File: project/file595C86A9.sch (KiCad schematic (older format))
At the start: 12 parts

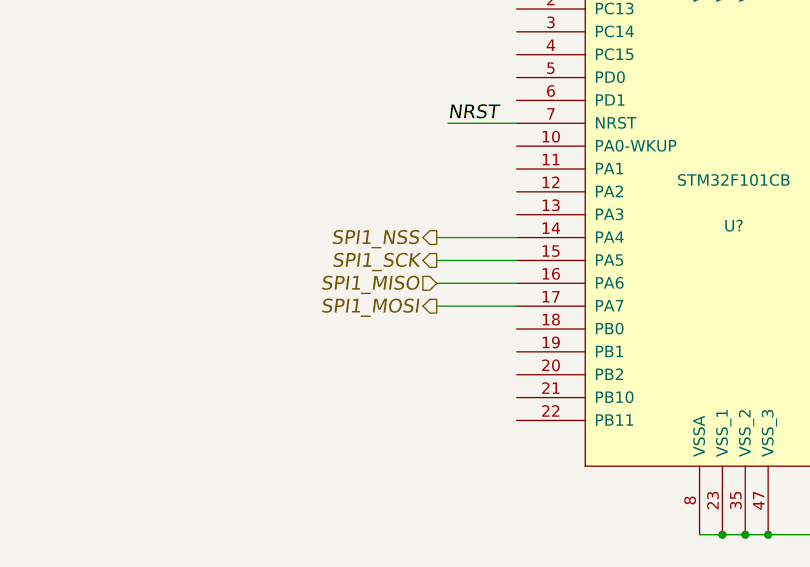
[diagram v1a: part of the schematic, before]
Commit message: Add AD5689R dual-channel DAC to schematic.
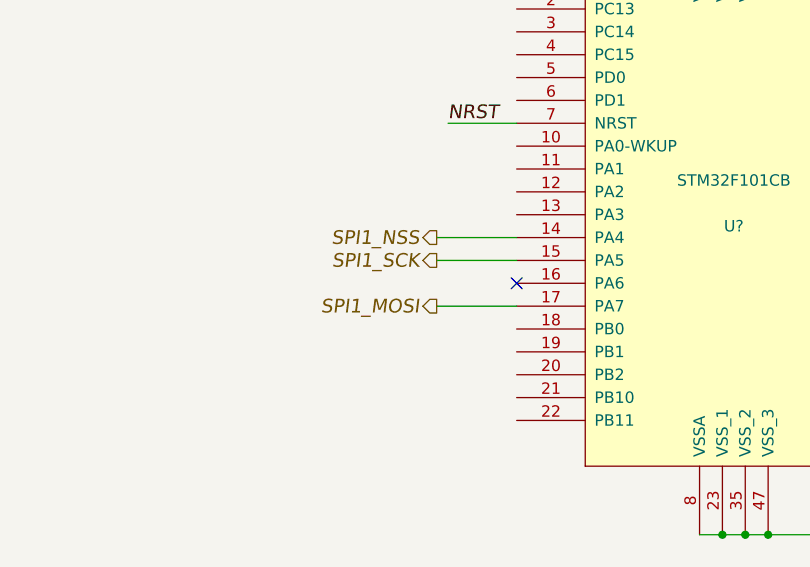
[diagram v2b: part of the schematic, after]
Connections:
- net SPI1_MISO: no longer names the net of U?.16 (PA6)
- no-connect marks 0 -> 1
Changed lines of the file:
@@
 $Descr A4 11693 8268
 encoding utf-8
-Sheet 2 5
+Sheet 2 6
 Title ""
 Date ""
@@
 $EndComp
 $Comp
-L +3.3V #PWR?
+L +3.3V #PWR03
 U 1 1 595C87F5
 P 5850 2050
-F 0 "#PWR?" H 5850 1900 50  0001 C CNN
+F 0 "#PWR03" H 5850 1900 50  0001 C CNN
 F 1 "+3.3V" H 5850 2190 50  0000 C CNN
 F 2 "" H 5850 2050 50  0001 C CNN
@@
 $EndComp
 $Comp
-L +3.3V #PWR?
+L +3.3V #PWR04
 U 1 1 595C8815
 P 6550 1450
-F 0 "#PWR?" H 6550 1300 50  0001 C CNN
+F 0 "#PWR04" H 6550 1300 50  0001 C CNN
 F 1 "+3.3V" H 6550 1590 50  0000 C CNN
 F 2 "" H 6550 1450 50  0001 C CNN
@@
 $EndComp
 $Comp
-L GND #PWR?
+L GND #PWR05
 U 1 1 595C8A05
 P 6550 1800
-F 0 "#PWR?" H 6550 1550 50  0001 C CNN
+F 0 "#PWR05" H 6550 1550 50  0001 C CNN
 F 1 "GND" H 6550 1650 50  0000 C CNN
 F 2 "" H 6550 1800 50  0001 C CNN
@@
 NRST
 $Comp
-L GND #PWR?
+L GND #PWR06
 U 1 1 595C8D73
 P 8700 1650
-F 0 "#PWR?" H 8700 1400 50  0001 C CNN
+F 0 "#PWR06" H 8700 1400 50  0001 C CNN
 F 1 "GND" H 8700 1500 50  0000 C CNN
 F 2 "" H 8700 1650 50  0001 C CNN
@@
 	6950 3000 6650 3000
 $Comp
-L GND #PWR?
+L GND #PWR07
 U 1 1 595C9081
 P 1350 1750
-F 0 "#PWR?" H 1350 1500 50  0001 C CNN
+F 0 "#PWR07" H 1350 1500 50  0001 C CNN
 F 1 "GND" H 1350 1600 50  0000 C CNN
 F 2 "" H 1350 1750 50  0001 C CNN
@@
 	1350 1450 1350 1350
 $Comp
-L +3.3V #PWR?
+L +3.3V #PWR08
 U 1 1 595C9179
 P 1350 1050
-F 0 "#PWR?" H 1350 900 50  0001 C CNN
+F 0 "#PWR08" H 1350 900 50  0001 C CNN
 F 1 "+3.3V" H 1350 1190 50  0000 C CNN
 F 2 "" H 1350 1050 50  0001 C CNN
@@
 	6950 4200 6650 4200
 $Comp
-L GND #PWR?
+L GND #PWR09
 U 1 1 595C9945
 P 6100 5300
-F 0 "#PWR?" H 6100 5050 50  0001 C CNN
+F 0 "#PWR09" H 6100 5050 50  0001 C CNN
 F 1 "GND" H 6100 5150 50  0000 C CNN
 F 2 "" H 6100 5300 50  0001 C CNN
@@
 Text HLabel 4400 4000 0    60   Output Italic 0
 SPI1_SCK
-Text HLabel 4400 4100 0    60   Input Italic 0
-SPI1_MISO
 Text HLabel 4400 4200 0    60   Output Italic 0
 SPI1_MOSI
@@
 Wire Wire Line
 	4400 4000 4750 4000
-Wire Wire Line
-	4400 4100 4750 4100
 Wire Wire Line
 	4400 4200 4750 4200
@@
 $EndComp
 $Comp
-L +3.3V #PWR?
+L +3.3V #PWR010
 U 1 1 595CA28A
 P 1650 2000
-F 0 "#PWR?" H 1650 1850 50  0001 C CNN
+F 0 "#PWR010" H 1650 1850 50  0001 C CNN
 F 1 "+3.3V" H 1650 2140 50  0000 C CNN
 F 2 "" H 1650 2000 50  0001 C CNN
@@
 	1300 2250 2050 2250
 $Comp
-L +3.3V #PWR?
+L +3.3V #PWR011
 U 1 1 595CA48A
 P 1650 2550
-F 0 "#PWR?" H 1650 2400 50  0001 C CNN
+F 0 "#PWR011" H 1650 2400 50  0001 C CNN
 F 1 "+3.3V" H 1650 2690 50  0000 C CNN
 F 2 "" H 1650 2550 50  0001 C CNN
@@
 	1    0    0    -1
 $EndComp
+NoConn ~ 4750 4100
 $EndSCHEMATC
